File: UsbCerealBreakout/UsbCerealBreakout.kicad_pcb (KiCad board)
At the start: 2 copper layers, 23.5 x 19 mm, 3 parts, among them J1 Serial Connector, J2 USB_C_Data_Output, P1 USB_C_Plug

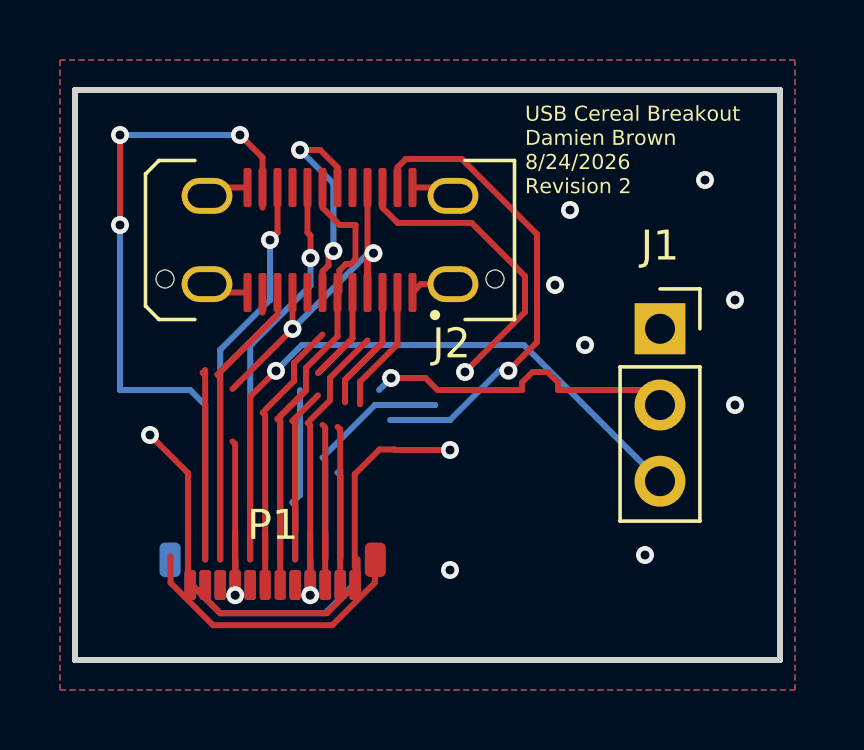
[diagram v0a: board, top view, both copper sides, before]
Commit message: Updated board with new USB C footprint, fixed several trace issues
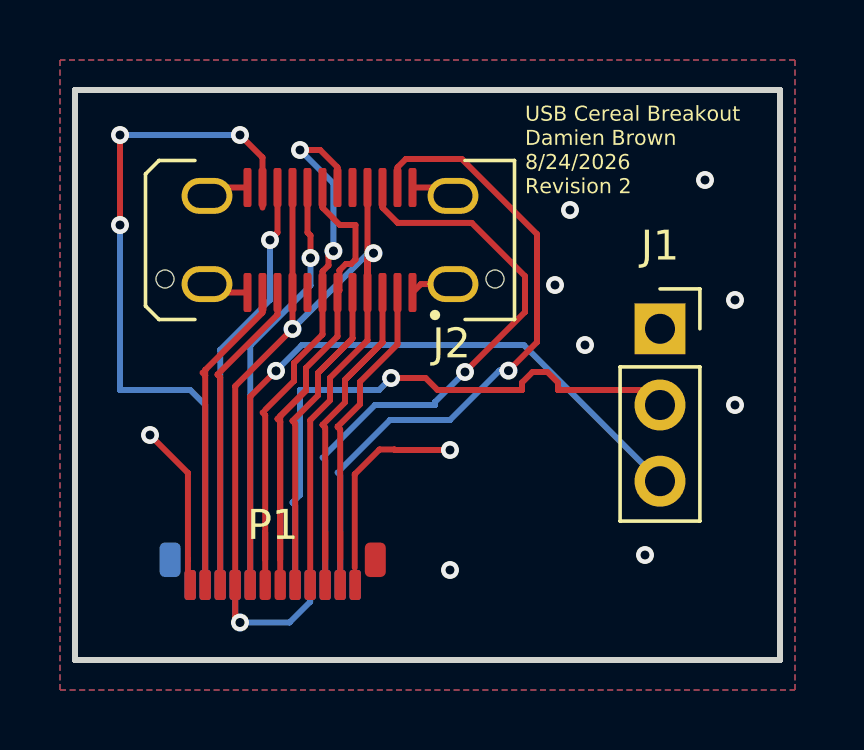
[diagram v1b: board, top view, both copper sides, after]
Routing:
- net GND: track 33.2 -> 17.9 mm
- net (no net): track 9.73 -> 0.00 mm
- net Net-(J2-VBUS-PadA4): track 31.9 -> 39.1 mm, vias 4 -> 3
- net Net-(J2-RX2+): track 7.11 -> 10.7 mm
- net Net-(J1-Pin_2): track 16.7 -> 20.2 mm
- net Net-(J2-RX1-): track 20.3 -> 22.6 mm
- net Net-(J2-CC1): track 14.4 -> 12.2 mm
- net Net-(P1-D-): track 17.5 -> 18.9 mm
- net Net-(J2-RX2-): track 11.7 -> 10.6 mm
- net Net-(J2-RX1+): track 21.5 -> 22.5 mm
- net Net-(J2-TX2-): track 13.2 -> 14.0 mm
- net Net-(J2-TX2+): track 23.4 -> 24.3 mm
- net Net-(J2-CC2): track 13.3 -> 14.1 mm
- net Net-(J1-Pin_3): track 21.7 -> 22.5 mm
- net Net-(J2-TX1-): track 12.7 -> 13.3 mm

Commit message: hopefully fixed more routing issues
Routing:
- net GND: track 17.9 -> 5.96 mm, vias 10 -> 8
- net Net-(P1-D+): track 21.7 -> 15.7 mm
- net Net-(J2-TX1-): track 13.3 -> 10.5 mm
- net Net-(J2-CC1): track 12.2 -> 10.5 mm
- net Net-(J2-TX2+): track 24.3 -> 25.8 mm
- net Net-(J2-TX1+): track 11.5 -> 10.5 mm
- net Net-(J1-Pin_2): track 20.2 -> 21.1 mm
- net Net-(P1-D-): track 18.9 -> 18.1 mm
- net Net-(J2-RX2-): track 10.6 -> 11.4 mm
- net Net-(J2-VBUS-PadA4): track 39.1 -> 38.6 mm, vias 3 -> 2

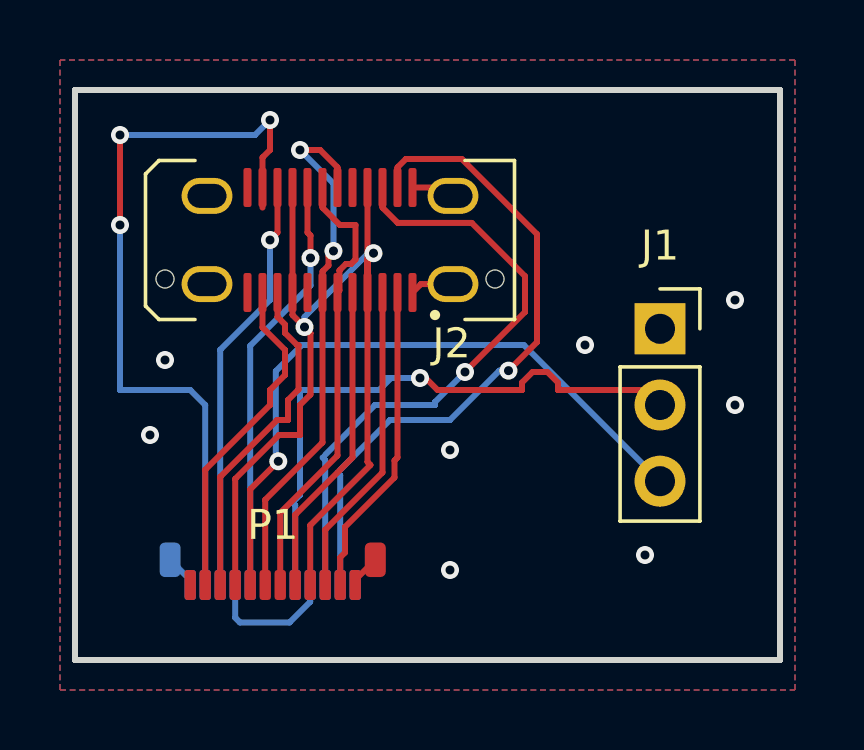
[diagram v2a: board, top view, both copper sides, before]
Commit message: Slight updates to fix branch problems, added VBUS via at USB connector
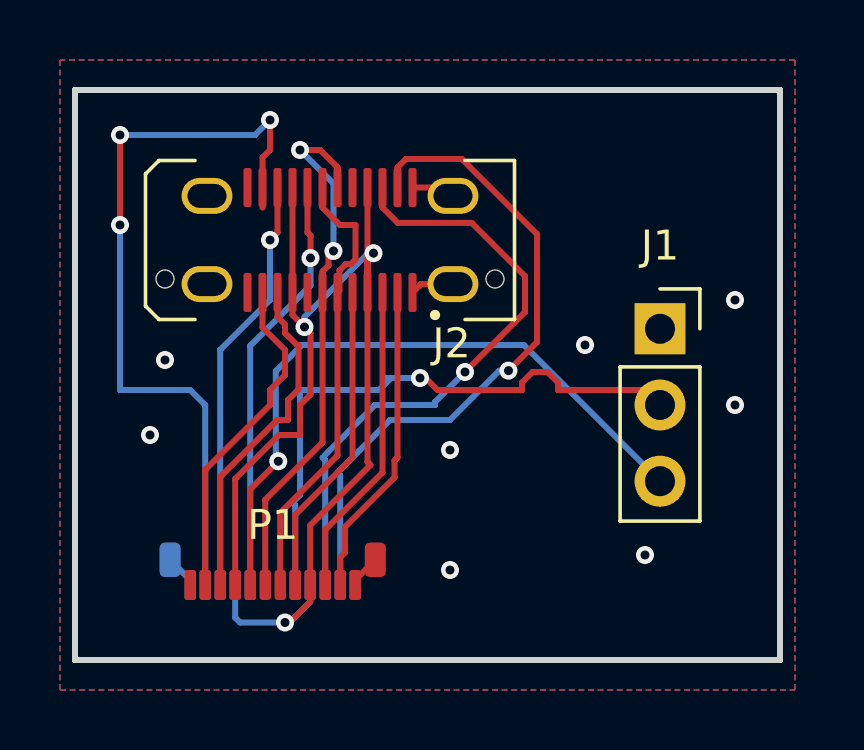
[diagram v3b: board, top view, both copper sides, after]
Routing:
- net Net-(J2-VBUS-PadA4): track 38.6 -> 40.3 mm, vias 2 -> 3
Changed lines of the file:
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@@
+	)
+	(segment
+		(start 130.34 81.561246)
+		(end 130.34 81)
+		(width 0.2)
+		(layer "F.Cu")
+		(net "Net-(J2-VBUS-PadA4)")
+	)
+	(segment
+		(start 129.5 82.25)
+		(end 129.651246 82.25)
+		(width 0.2)
+		(layer "F.Cu")
+		(net "Net-(J2-VBUS-PadA4)")
 	)
 	(segment
@@
 		(start 132.45 69.939326)
 		(end 132.45 69.95)
+		(width 0.2)
+		(layer "F.Cu")
+		(net "Net-(J2-VBUS-PadA4)")
+	)
+	(segment
+		(start 129.651246 82.25)
+		(end 130.34 81.561246)
 		(width 0.2)
 		(layer "F.Cu")
@@
 		(net "Net-(J2-VBUS-PadA4)")
 	)
+	(via
+		(at 129.5 82.25)
+		(size 0.6)
+		(drill 0.3)
+		(layers "F.Cu" "B.Cu")
+		(net "Net-(J2-VBUS-PadA4)")
+	)
 	(segment
 		(start 132.275186 69.939326)
@@
 	(segment
 		(start 129.651246 82.25)
+		(end 129.5 82.25)
+		(width 0.2)
+		(layer "B.Cu")
+		(net "Net-(J2-VBUS-PadA4)")
+	)
+	(segment
+		(start 129.5 82.25)
 		(end 128 82.25)
 		(width 0.2)
